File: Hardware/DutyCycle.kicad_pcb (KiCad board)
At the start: 2 copper layers, 37 parts, among them J1 LiPo, J2 USB, J4 MOT, Q1 AO3400A, Q2 AO3400A, Q3 AO3401A, SW1 SW_Push, U1 AT32F421KxU7, U3 ME6211C28M5, U5 TP4055

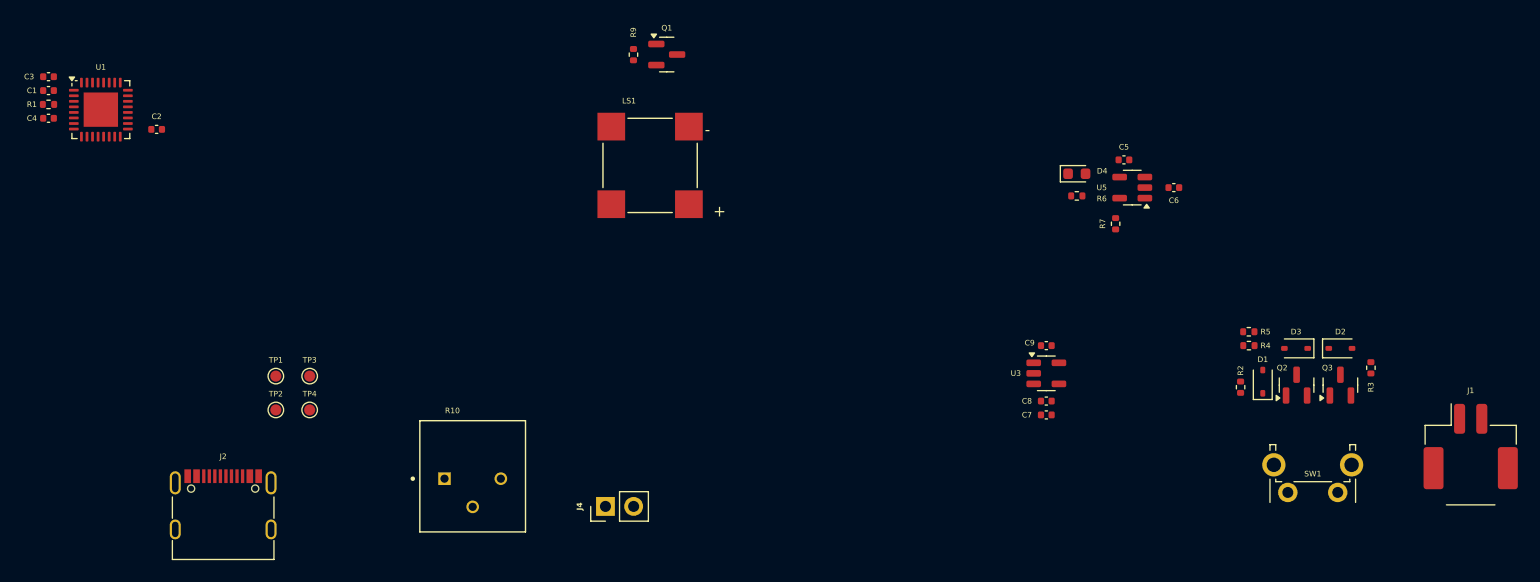
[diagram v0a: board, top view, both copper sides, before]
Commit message: feat(pcb): complete the basic layout of components
Signed-off-by: _VIFEXTech <vifextech@foxmail.com>
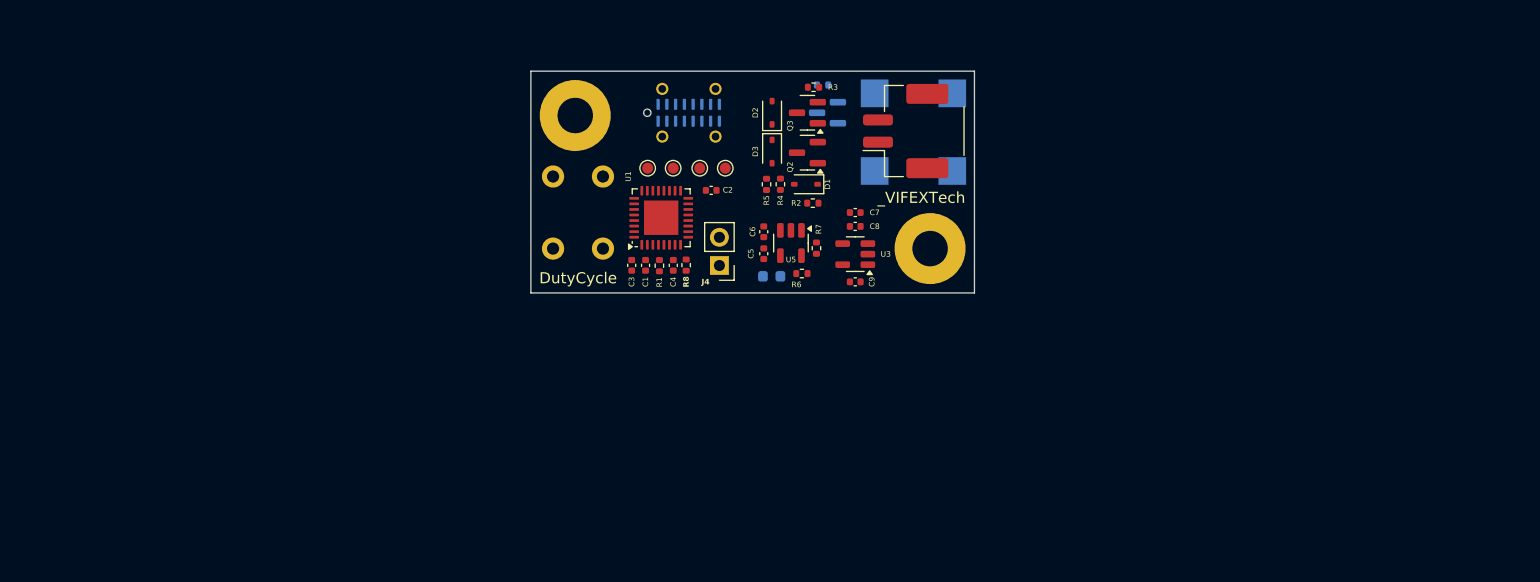
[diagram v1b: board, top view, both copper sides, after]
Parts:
- removed R10: 3296P-1-105, DutyCycle:TRIM_3296P-1-105
- added H1: MountingHole_Pad, MountingHole:MountingHole_3.2mm_M3_Pad, F.Cu at (79.0, 79.0)
- added H2: MountingHole_Pad, MountingHole:MountingHole_3.2mm_M3_Pad, F.Cu at (111.0, 91.0)
- added R8: 5.1kR, Resistor_SMD:R_0402_1005Metric, F.Cu at (89.0, 92.5)
- D4, LS1, Q1, R9: moved to B.Cu
- J2: footprint Connector_USB:USB_C_Receptacle_G-Switch_GT-USB-7010ASV -> Connector_USB:USB_C_Receptacle_G-Switch_GT-USB-7051x; moved to B.Cu
- SW1: footprint Button_Switch_THT:SW_Tactile_SPST_Angled_PTS645Vx83-2LFS -> Button_Switch_THT:SW_PUSH_6mm_H13mm; moved to B.Cu
- moved SW1 76.3 mm to (77.0, 84.5), turned to -90 degrees
- moved J1 58.4 mm to (108.8, 80.4), turned to 90 degrees
- moved C4 57.9 mm to (87.8, 92.5), turned to -90 degrees
- moved R1 57.0 mm to (86.6, 92.5), turned to 90 degrees
- moved R3 56.3 mm to (100.5, 76.5), turned to 180 degrees
- moved C1 56.1 mm to (85.3, 92.5), turned to -90 degrees
- moved J2 55.6 mm to (89.2, 78.8)
- moved D2 55.5 mm to (96.8, 78.8), turned to 90 degrees
- moved C3 55.3 mm to (84.1, 92.5), turned to -90 degrees
- moved Q3 54.0 mm to (99.9, 78.8), turned to 180 degrees
- moved U1 51.5 mm to (86.8, 88.2), turned to 90 degrees
- moved D3 50.5 mm to (96.8, 82.2), turned to -90 degrees
- moved C2 50.3 mm to (91.3, 85.8)
- moved Q2 48.8 mm to (99.9, 82.3), turned to 180 degrees
- moved R5 45.5 mm to (96.2, 85.2), turned to 90 degrees
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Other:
- board outline added: 40 x 20 mm
- board text added: "DutyCycle"
- board text added: "_VIFEXTech"

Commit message: feat(pcb): finish PCB layout
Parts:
- D4: moved to F.Cu
- moved D4 16.9 mm to (98.8, 76.8), turned to 0 degrees
- moved C5 13.7 mm to (101.2, 78.8), turned to -90 degrees
- moved R7 13.0 mm to (96.2, 78.8), turned to 90 degrees
- moved R6 12.9 mm to (96.2, 80.8), turned to 90 degrees
- moved U5 10.8 mm to (98.8, 79.8), turned to 90 degrees
- moved C6 10.1 mm to (101.2, 80.8), turned to 90 degrees
- moved D1 7.10 mm to (99.0, 92.2)
- moved Q2 7.07 mm to (99.4, 89.4)
- moved D2 7.07 mm to (96.2, 85.8)
- moved D3 7.07 mm to (96.2, 89.3)
- moved Q3 7.07 mm to (99.4, 85.8)
- moved R3 7.07 mm to (100.0, 83.5)
- moved R2 5.45 mm to (101.5, 92.2), turned to -90 degrees
- moved R9 4.45 mm to (102.2, 80.6)
- moved TP3 3.74 mm to (86.5, 83.5)
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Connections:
- J2 pad A5: /DEBUG_TX -> /SWCLK
- J2 pad A6: /DEBUG_RX -> /SWDIO
- J2 pad A7: /SWDIO -> /DEBUG_RX
- J2 pad A8: /SWCLK -> /DEBUG_TX
- J2 pad B5: /DEBUG_TX -> unconnected-(J2-CC2-PadB5)
- J2 pad B6: /DEBUG_RX -> unconnected-(J2-D+-PadB6)
- J2 pad B7: /SWDIO -> unconnected-(J2-D--PadB7)
- J2 pad B8: /SWCLK -> unconnected-(J2-SBU2-PadB8)
- U1 pad 13: unconnected-(U1-PA7-Pad13) -> /PWR_EN
- U1 pad 14: /MOT_OUT1 -> /KEY_DET
- U1 pad 15: /MOT_OUT2 -> /BAT_DET
- U1 pad 16: unconnected-(U1-PB2-Pad16) -> /BUZZ
- U1 pad 25: /PWR_EN -> unconnected-(U1-PA15-Pad25)
- U1 pad 26: /KEY_DET -> unconnected-(U1-PB3-Pad26)
- U1 pad 6: /BAT_DET -> unconnected-(U1-PA0-Pad6)
- U1 pad 7: /BUZZ -> unconnected-(U1-PA1-Pad7)
- U1 pad 8: unconnected-(U1-PA2-Pad8) -> /MOT_OUT1
- U1 pad 9: unconnected-(U1-PA3-Pad9) -> /MOT_OUT2
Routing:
- net VDD: track 0.00 -> 47.9 mm, vias 0 -> 2
- net Net-(D2-K): track 0.00 -> 25.7 mm, vias 0 -> 1
- net VBAT: track 0.00 -> 21.8 mm, vias 0 -> 1
- net VBUS: track 0.00 -> 21.8 mm, vias 0 -> 2
- net /BUZZ: track 0.00 -> 21.0 mm, vias 0 -> 1
- net Net-(D2-A): track 0.00 -> 11.9 mm, vias 0 -> 2
- net /BAT_IN: track 0.00 -> 10.8 mm
- net /PWR_EN: track 0.00 -> 10.5 mm
- net /DEBUG_RX: track 0.00 -> 9.94 mm, vias 0 -> 1
- net /SWCLK: track 0.00 -> 9.61 mm, vias 0 -> 1
- net /DEBUG_TX: track 0.00 -> 9.52 mm, vias 0 -> 1
- net /SWDIO: track 0.00 -> 8.80 mm, vias 0 -> 1
- net /KEY_DET: track 0.00 -> 8.26 mm
- net /BAT_DET: track 0.00 -> 6.61 mm
- net Net-(D4-K): track 0.00 -> 6.15 mm
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- added copper zone on B.Cu, net GND
- added copper zone on F.Cu, net GND
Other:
- board text added: "${TITLE}"
- board text added: "+"
- board text added: "-"
- board text added: "CC=CLK D-=RX D+=DIO SBU=TX"
- board text added: "CHG"
- board text added: "CLK"
- board text added: "DIO"
- board text added: "REV: ${REVISION} ${CURRENT_DATE}"
- board text added: "RX"
- board text added: "TX"
- board text removed: "DutyCycle"

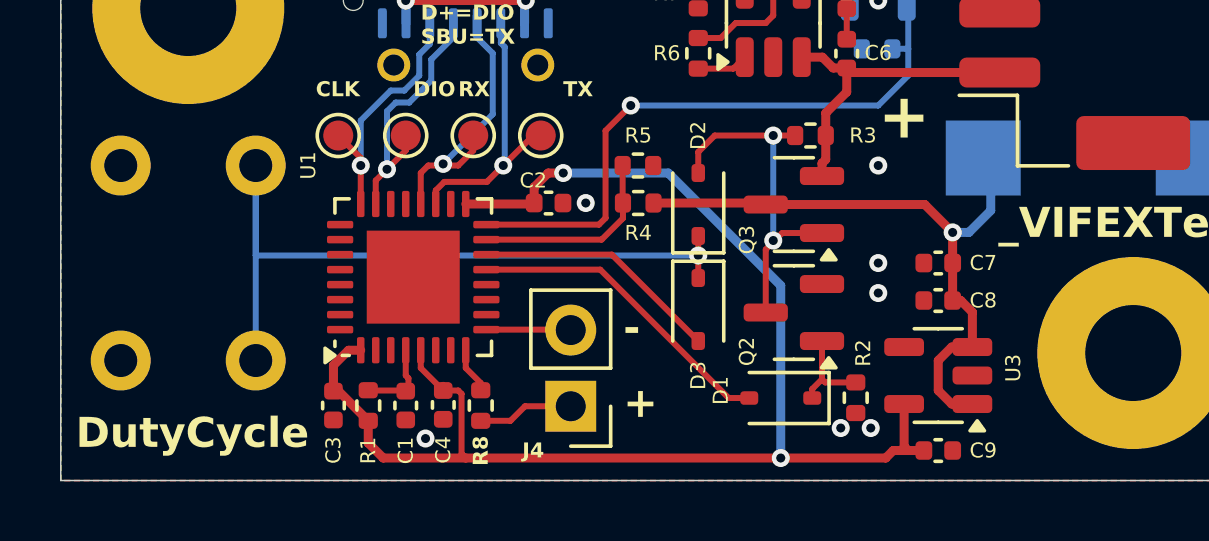
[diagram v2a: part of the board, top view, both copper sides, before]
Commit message: feat(Hardware): add external crystal & fix LDO packaging errors
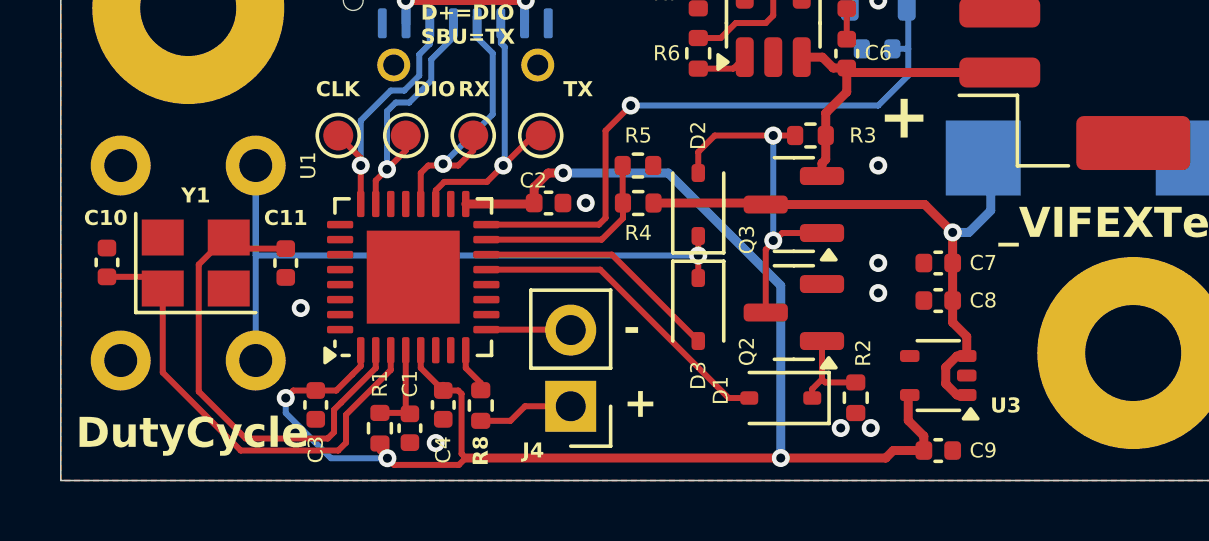
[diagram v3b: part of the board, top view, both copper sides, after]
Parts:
- added C10: 10pF, Capacitor_SMD:C_0402_1005Metric, F.Cu at (76.5, 87.7)
- added C11: 10pF, Capacitor_SMD:C_0402_1005Metric, F.Cu at (82.5, 87.8)
- added Y1: Crystal_GND24, Crystal:Crystal_SMD_3225-4Pin_3.2x2.5mm, F.Cu at (79.5, 87.8)
- R8: value 5.1kR -> 2kR
- U3: footprint Package_TO_SOT_SMD:SOT-23-5 -> Package_TO_SOT_SMD:SOT-353_SC-70-5
- moved R1 0.85 mm to (85.6, 93.3)
- moved C1 0.77 mm to (86.6, 93.3)
- moved C3 0.59 mm to (83.5, 92.5)
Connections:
- U1 pad 2: unconnected-(U1-HEXT_OUT/PF0-Pad2) -> /HEXT_OUT
- U1 pad 3: unconnected-(U1-HEXT_IN/PF1-Pad3) -> /HEXT_IN
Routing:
- net /HEXT_OUT: track 0.00 -> 16.2 mm
- net /HEXT_IN: track 0.00 -> 15.8 mm
- net VDD: track 47.9 -> 52.4 mm, vias 2 -> 4
- net VBAT: track 21.8 -> 20.5 mm
- net /RST: track 2.63 -> 3.19 mm
- net GND: track 1.11 -> 1.07 mm, vias 10 -> 11
